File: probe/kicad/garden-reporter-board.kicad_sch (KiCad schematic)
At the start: 26 parts, among them J1 70543-0106, J2 Conn_01x02, J3 70543-0002, J4 70543-0002, J5 70543-0002, Q1 TN0702N3-G, U1 MCP1700-3302E_TO92, U2 MCP1700-3302E_TO92, U3 MCP1700-1202E_TO92

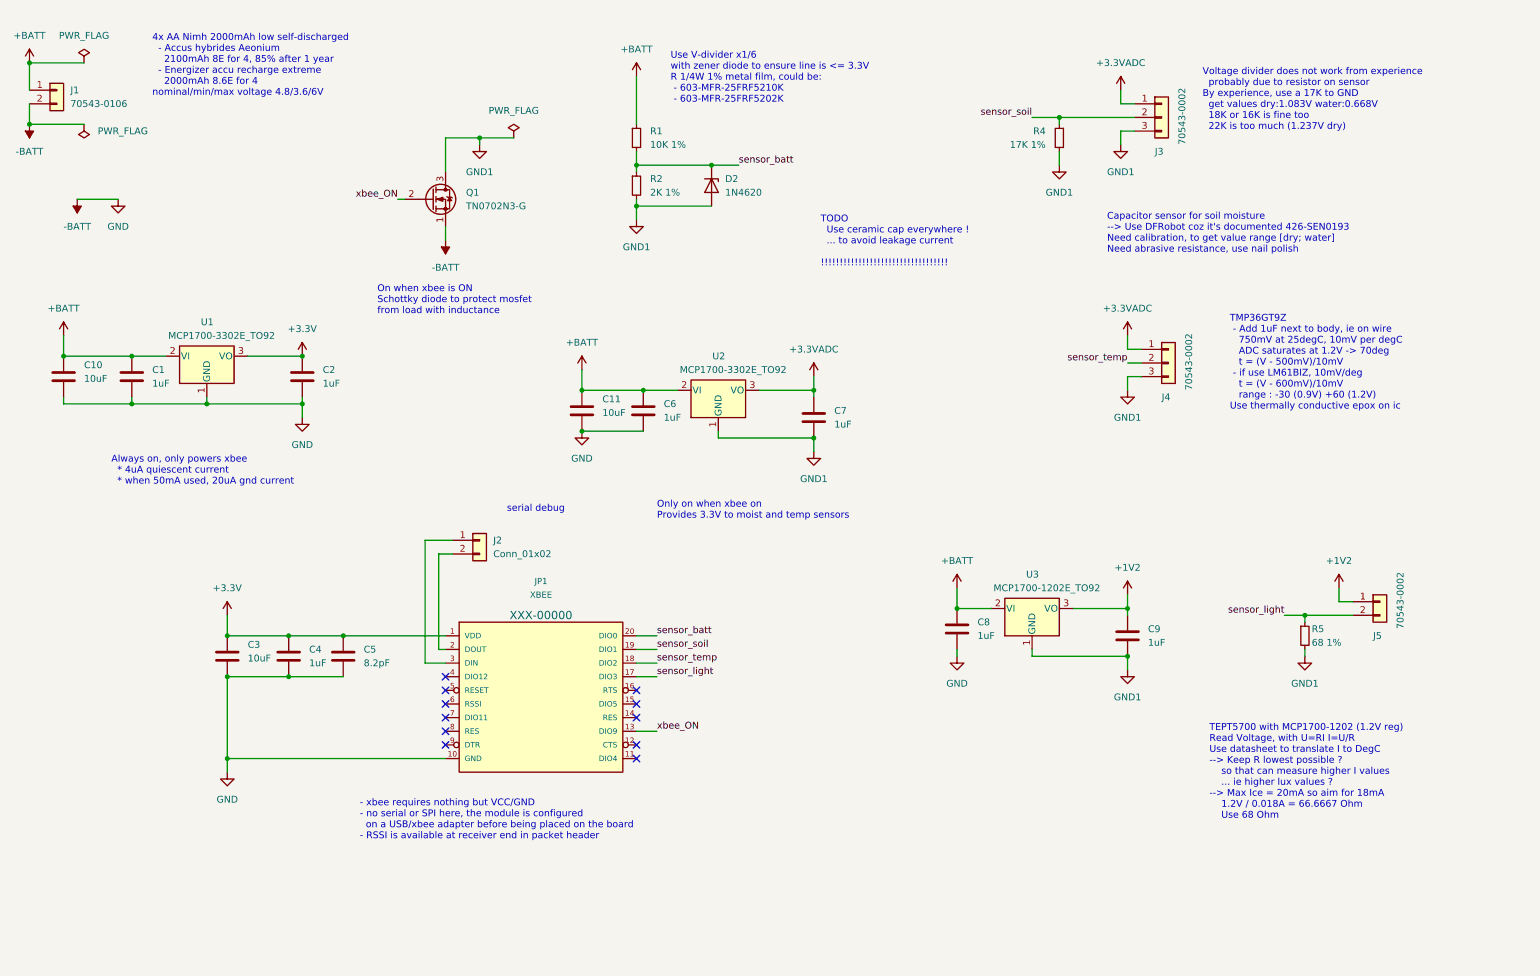
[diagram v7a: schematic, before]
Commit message: Use high side switch, chose new components and footprints, layed out but no route, use GND plane, add doc and datasheet
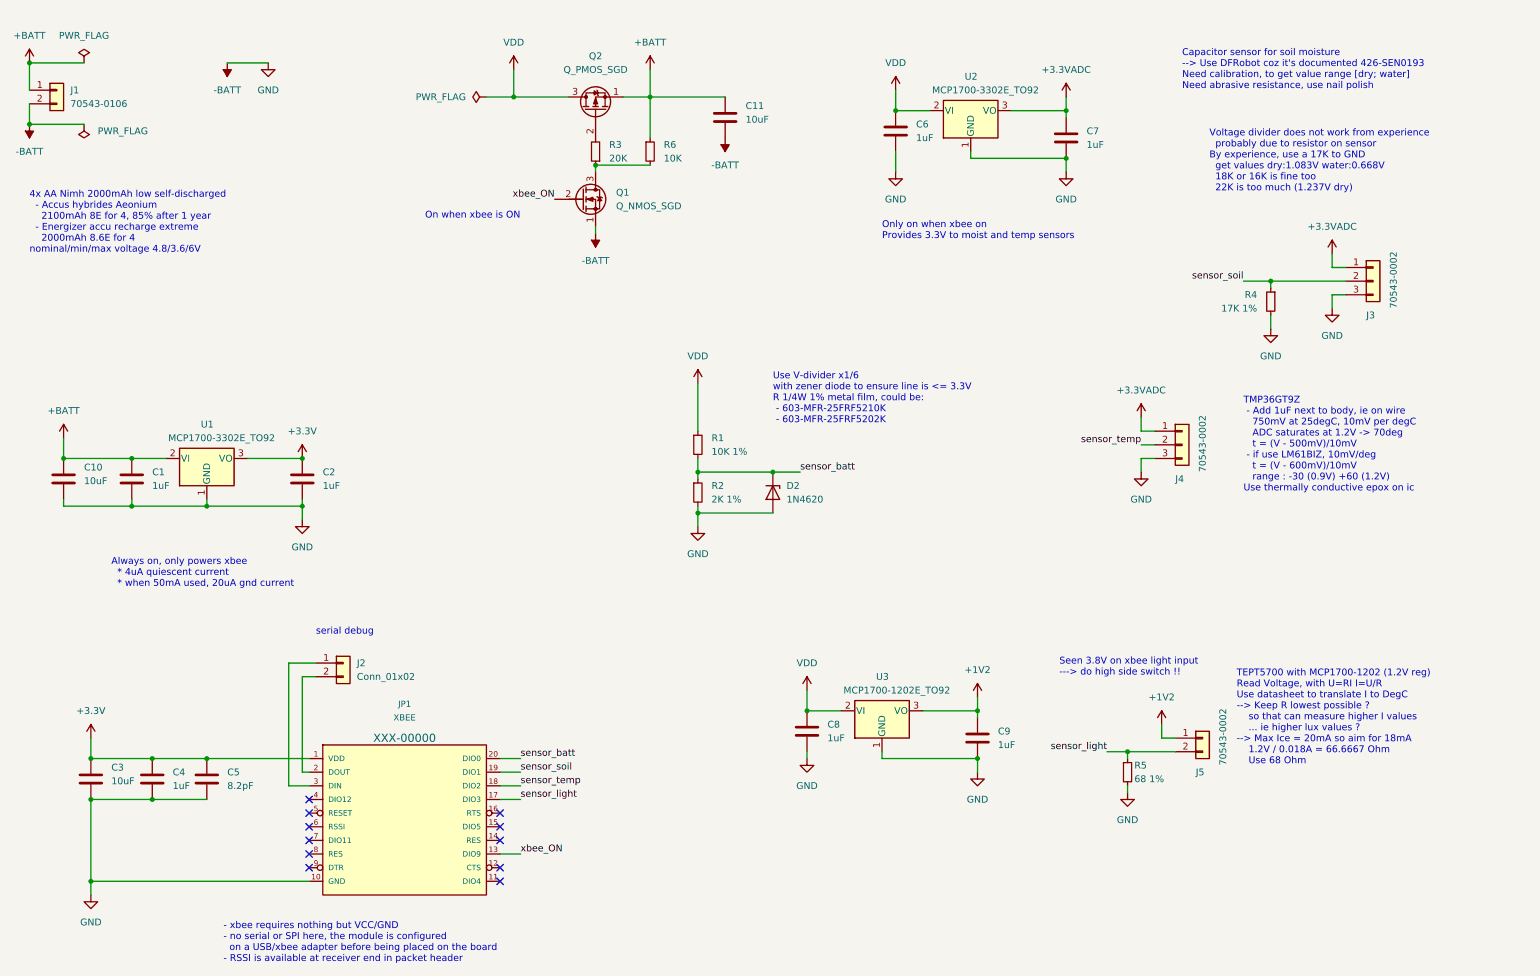
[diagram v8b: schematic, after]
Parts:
- removed Q1: TN0702N3-G, Package_TO_SOT_THT:TO-92_Inline, symbol Device:Q_NMOS_DGS
- added Q1: Q_NMOS_SGD, Package_TO_SOT_THT:TO-92_Inline, symbol Device:Q_NMOS_SGD
- added Q2: Q_PMOS_SGD, Package_TO_SOT_THT:TO-92_Inline, symbol Device:Q_PMOS_SGD
- added R3: 20K, Resistor_THT:R_Axial_DIN0207_L6.3mm_D2.5mm_P7.62mm_Horizontal, symbol Device:R_Small
- added R6: 10K, Resistor_THT:R_Axial_DIN0207_L6.3mm_D2.5mm_P7.62mm_Horizontal, symbol Device:R_Small
- C1, C2, C4, C6, C7, C8, C9: mouser (none) -> FG18X5R1H105KRT06
- C10, C11, C3: mouser (none) -> 810-FG18X5R1E106MR06
- C5: mouser (none) -> 80-C315C829D2G
- D2: mouser (none) -> 610-1N4620BK
- J1, J5: mouser (none) -> 538-70543-0106
- J3, J4: mouser (none) -> 538-70543-0002
- JP1: footprint XBEE -> RF-SF:XBEE; mouser (none) -> 710-62001011821
- R1: mouser (none) -> 603-MFR-25FRF5210K
- R2: mouser (none) -> 603-MFR-25FRF522K
- R4: mouser (none) -> 603-MFR-25FTF52-17K
- R5: mouser (none) -> 279-LR0204F68R
- U1, U2: farnell (none) -> 1296588; mouser (none) -> 579-MCP1700-3302E/TO
- U3: mouser (none) -> 579-MCP1700-1202E/TO
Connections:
- net GND1 is gone; now on net -BATT: C7.2, C9.2, D2.2 (A), J3.3 (Pin_3), J4.3 (Pin_3), R2.2, R4.2, R5.2, U2.1 (GND), U3.1 (GND)
- net +BATT: now also Q2.1 (S), R6.1; no longer C6.1, C8.1, R1.1, U2.2 (VI), U3.2 (VI)
- net -BATT: now also Q1.1 (S)
- net xbee_ON: now also Q1.2 (G)
- new net: Q2.2 (G), R3.2
- new net: Q1.3 (D), R3.1, R6.2
- new net VDD: C6.1, C8.1, Q2.3 (D), R1.1, U2.2 (VI), U3.2 (VI)
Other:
- note added: "On when xbee is ON"
- note added: "Seen 3.8V on xbee light input ---> do high side switch !!"
- note removed: "On when xbee is ON Schottky diode to protect mosfet from load with inductance"
- note removed: "TODO Use ceramic cap everywhere ! ... to avoid leakage current !!!!!!!!!!!!!!!!!!!!!!!!!!!!!!!!!!"
- moved on the sheet: C1, C10, C2, C4, C5, C6, C7, C8, C9, D2, J2, J3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
